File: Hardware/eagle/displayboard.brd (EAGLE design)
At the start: 70.8 x 45.7 mm, 11 parts, among them J1 CON_HEADER_1X08-SMD, J2 FH12-10S-0.5SH, J3 CON_HEADER_1X08-SMD

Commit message: Update to board design
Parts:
- added I2C, UART: CON_HEADER_1X04, dp_devices.v6:M1X4
- added R1: 100k, rcl:R0805
- CN1: device adafruit:JST-PH-2-SMT-RA -> pinhead:1X02
- moved CN1 53.4 mm to (63.5, 26.7), turned to 180 degrees
- moved J1 14.9 mm to (53.3, 44.5)
- moved J3 14.9 mm to (27.9, 44.5)
- moved C1 11.4 mm to (30.4, 24.3)
- moved C2 11.4 mm to (36.3, 26.8)
- moved C3 11.4 mm to (30.5, 27.9)
- moved C4 11.4 mm to (39.9, 26.7)
- moved U$1 10.2 mm to (30.4, 18.7)
- moved J2 5.22 mm to (40.6, 6.42)
- moved U$2 5.08 mm to (40.6, 22.9)
- moved BT1 4.58 mm to (39.4, 6.35), flipped to the bottom
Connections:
- removed net N$12: J3.6
- removed net N$13: J3.7
- removed net N$14: J3.8
- removed net N$3: BT1.PWR@1, CN1.1
- removed net N$8: J1.8
- new net RX: J3.7, UART.3
- new net SCL: I2C.2, J1.8
- new net SDA: I2C.3, J3.8
- new net TX: J3.6, UART.2
- new net V+: BT1.PWR@1, CN1.2, J1.6
- net DISP_EN: now also R1.1
- net GND: now also I2C.4, R1.2, UART.4
- net N$5: now also CN1.1; no longer CN1.2
- net VCC: now also I2C.1, UART.1
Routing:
- net N$5: track 0.00 -> 65.6 mm
- net GND: track 113.3 -> 54.4 mm, vias 0 -> 1
- net VCC: track 42.1 -> 96.2 mm, vias 0 -> 1
- net V+: track 0.00 -> 45.5 mm
- net SDA: track 0.00 -> 36.0 mm, vias 0 -> 2
- net DISP_EN: track 44.1 -> 66.3 mm
- net VDD: track 22.8 -> 40.2 mm
- net MOSI: track 34.4 -> 50.3 mm
- net CS: track 32.7 -> 48.2 mm
- net EXTCOM: track 28.3 -> 43.5 mm
- net SCLK: track 29.7 -> 44.1 mm
- net TX: track 0.00 -> 13.4 mm, vias 0 -> 1
- net RX: track 0.00 -> 9.04 mm, vias 0 -> 2
- net SCL: track 0.00 -> 7.77 mm, vias 0 -> 1
- net N$2: track 4.54 -> 5.81 mm
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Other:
- board size 70.8 x 45.7 mm -> 81 x 55.9 mm
- board text added: "+"
- board text added: "-"
- board text added: "A Hack-A-Gecko project"
- board text added: "Meeting Room Monitor"
- board text added: "RX"
- board text added: "SCL"
- board text added: "SDA"
- board text added: "TX"
- board text added: "by Steven Cooreman"

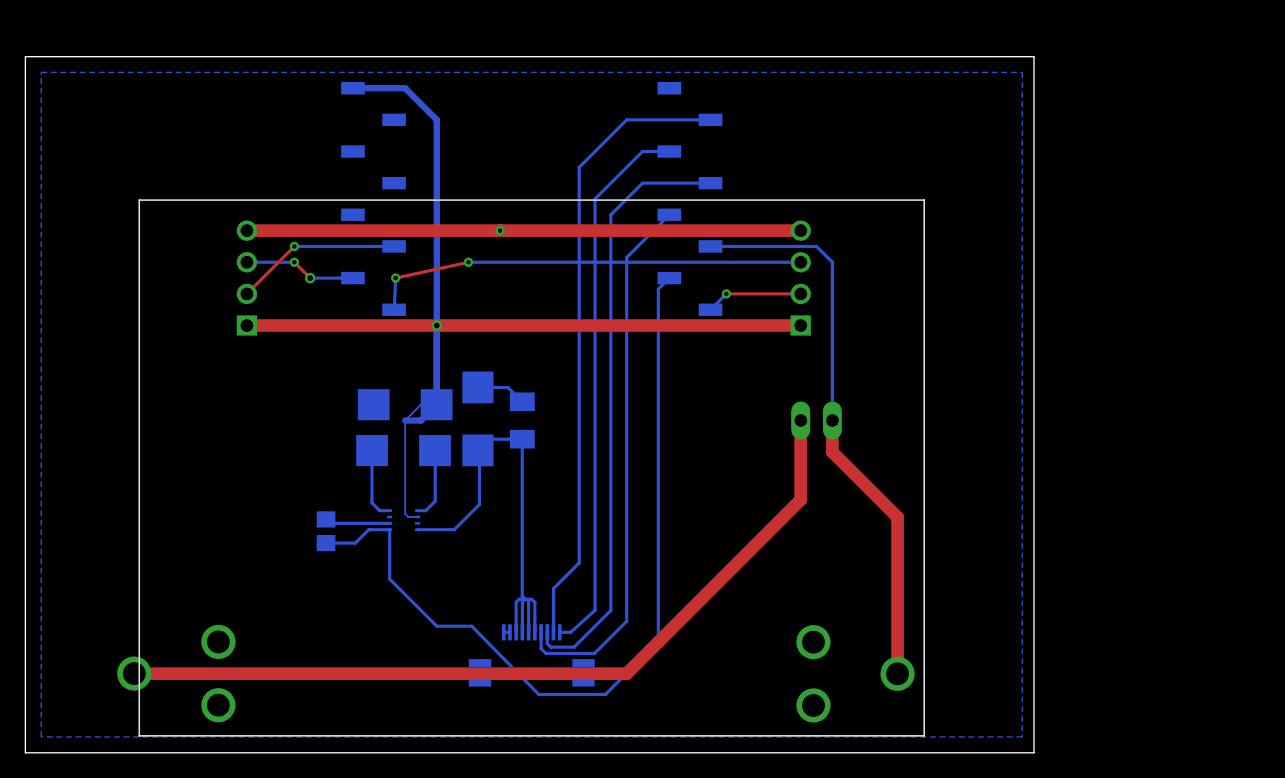
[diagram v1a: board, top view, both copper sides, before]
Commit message: Fixup board routing & add EEPROM for identity storage
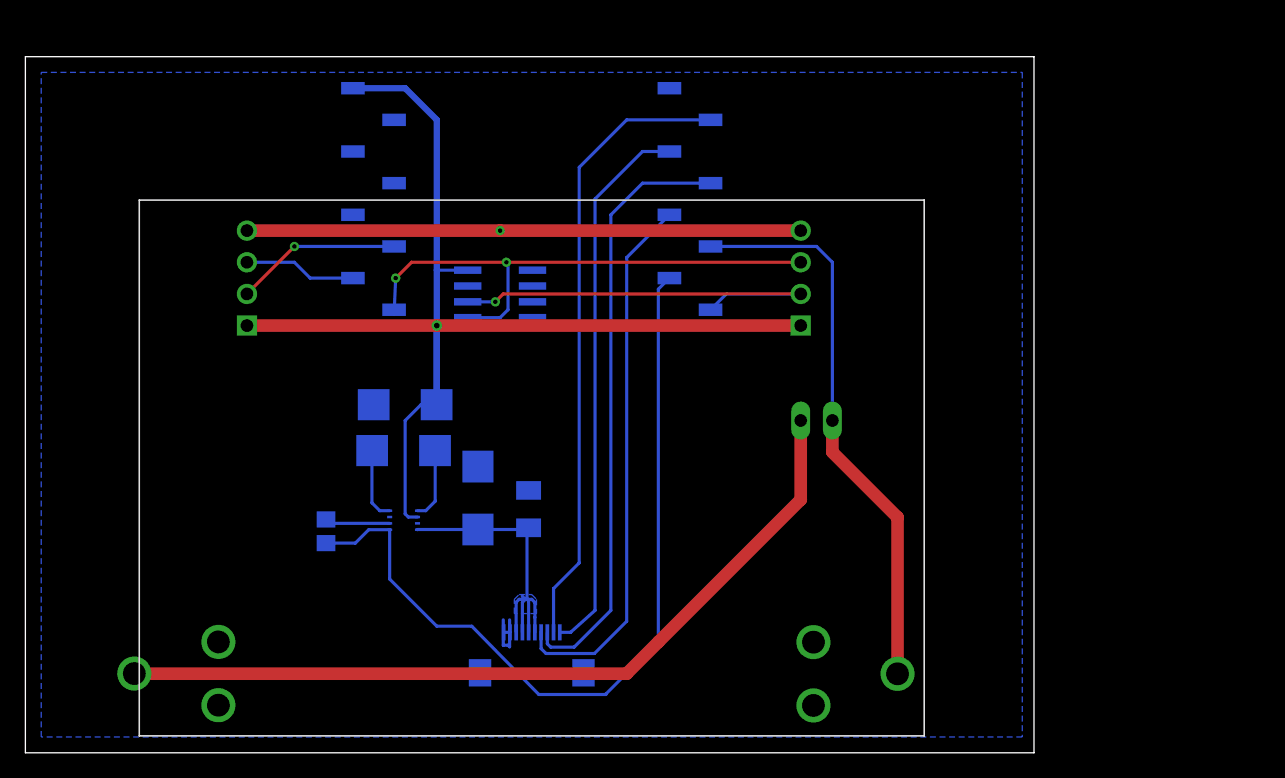
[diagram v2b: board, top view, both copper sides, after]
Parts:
- added IC1: 24C16, microchip:SO-08
- moved C4 7.13 mm to (40.4, 19.6)
- moved C2 6.35 mm to (36.3, 20.4)
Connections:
- net GND: now also IC1.4, IC1.7
- net SCL: now also IC1.6
- net SDA: now also IC1.5
- net VCC: now also IC1.8
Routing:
- net SCL: track 7.77 -> 34.8 mm
- net VDD: track 40.2 -> 28.1 mm
- net SDA: track 36.0 -> 43.8 mm
- net GND: track 54.4 -> 55.1 mm
- net VCC: track 96.2 -> 95.6 mm
- net RX: vias 2 -> 0
- added copper zone on layer 16, net VDD

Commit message: Spin a fixed board revision
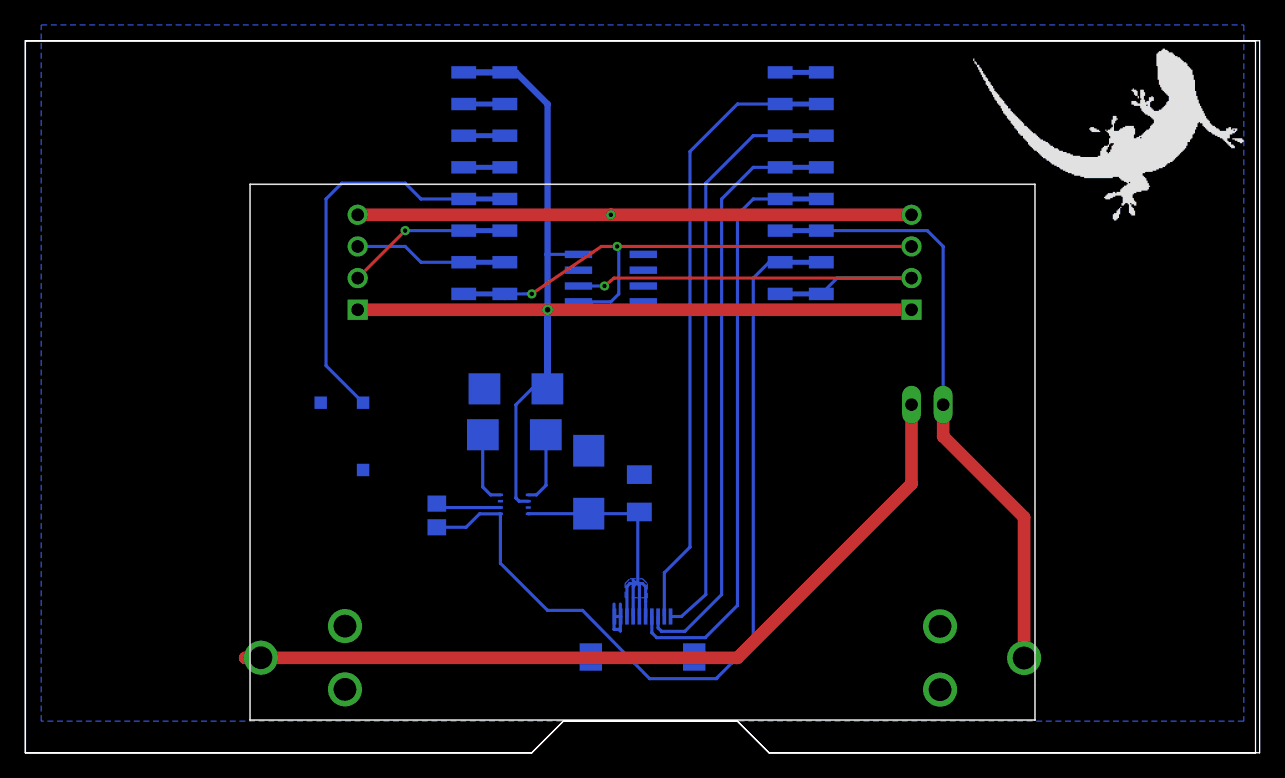
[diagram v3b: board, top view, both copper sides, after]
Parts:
- added SPK1: SMT-0540-S-R, adafruit:SMT-0540-S-R
- J1, J3: value CON_HEADER_1X08-SMD -> (none); device dp_devices.v6:M1X8_SMD -> SparkFun-Connectors:1X08_SMD_COMBINED
- moved J3 13.5 mm to (36.8, 54.6)
- moved J1 13.5 mm to (62.2, 54.6)
- moved BT1 10.2 mm to (49.5, 7.62)
- moved I2C 8.98 mm to (71.1, 35.6)
- moved R1 8.98 mm to (33.0, 19.1)
- moved C1 8.98 mm to (39.2, 25.5)
- moved C2 8.98 mm to (45.2, 21.7)
- moved C4 8.98 mm to (49.3, 20.8)
- moved CN1 8.98 mm to (72.4, 27.9)
- moved IC1 8.98 mm to (47.0, 38.1)
- moved J2 8.98 mm to (49.5, 7.69)
- moved U$1 8.98 mm to (39.2, 19.9)
- moved U$2 8.98 mm to (49.5, 24.1)
- moved UART 8.98 mm to (26.7, 35.6)
- moved C3 8.98 mm to (39.4, 29.2)
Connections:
- removed net N$11: J3.5
- new net BUZZ: J3.5, SPK1.+
- net GND: now also SPK1.-
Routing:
- net BUZZ: track 0.00 -> 29.7 mm
- net SDA: track 43.8 -> 41.6 mm
- net EXTCOM: track 43.5 -> 44.7 mm
- net N$5: track 65.6 -> 66.9 mm
- net V+: track 45.5 -> 46.0 mm
- net DISP_EN: track 66.3 -> 66.8 mm
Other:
- board size 81 x 55.9 mm -> 99.1 x 57.1 mm
